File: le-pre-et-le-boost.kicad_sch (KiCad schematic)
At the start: 17 parts, among them J1 Power In, J2 IN, J3 OUT, Q1 MMBFJ201, Q2 MMBT5088

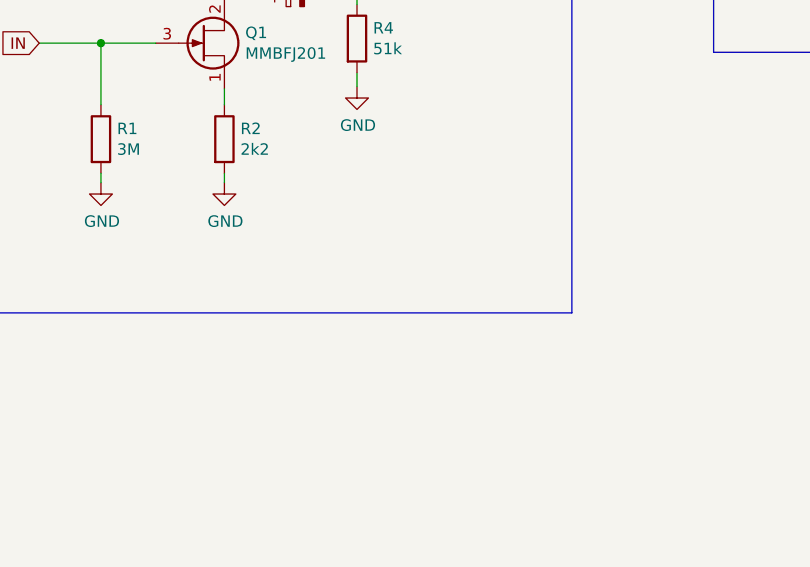
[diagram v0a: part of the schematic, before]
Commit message: some position and silkscreen adjustments
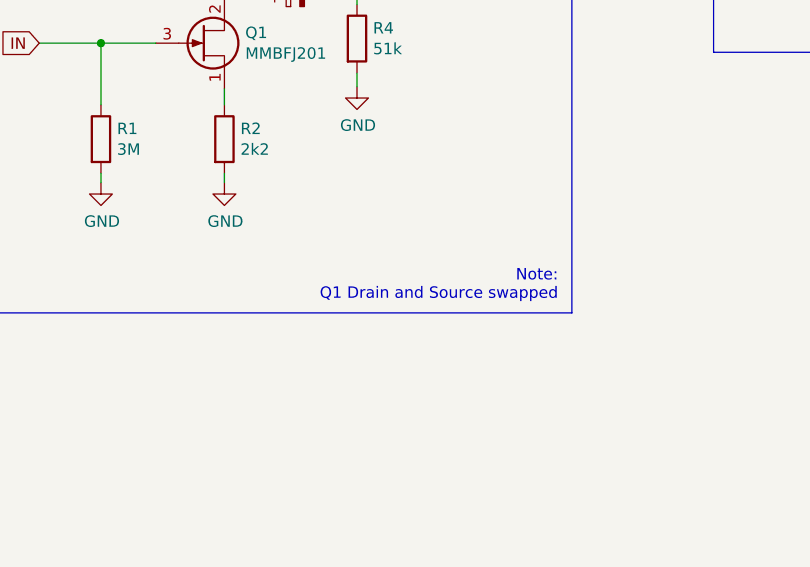
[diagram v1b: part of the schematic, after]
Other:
- note added: "Note: Q1 Drain and Source swapped"
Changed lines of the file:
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@@
+    (effects (font (size 1.27 1.27)) (justify right bottom))
+  )
+  (text "Note:\nQ1 Drain and Source swapped" (at 153.924 130.302 180)
     (effects (font (size 1.27 1.27)) (justify right bottom))
   )

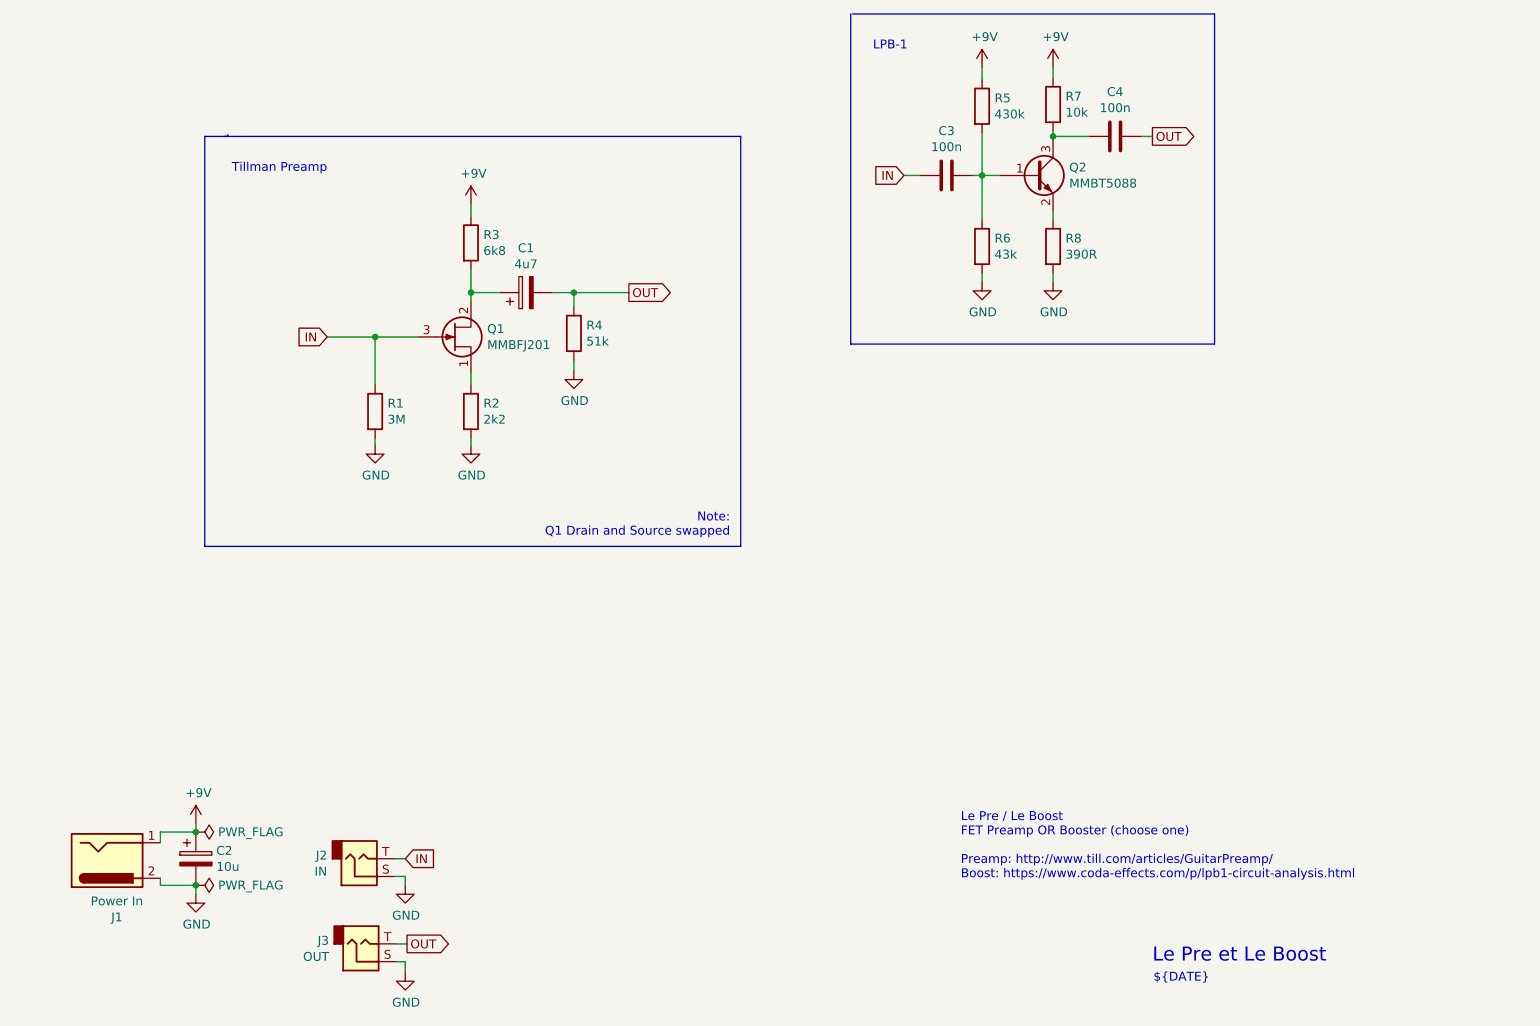
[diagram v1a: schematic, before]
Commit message: v0.2: THT footprints for electrolytics
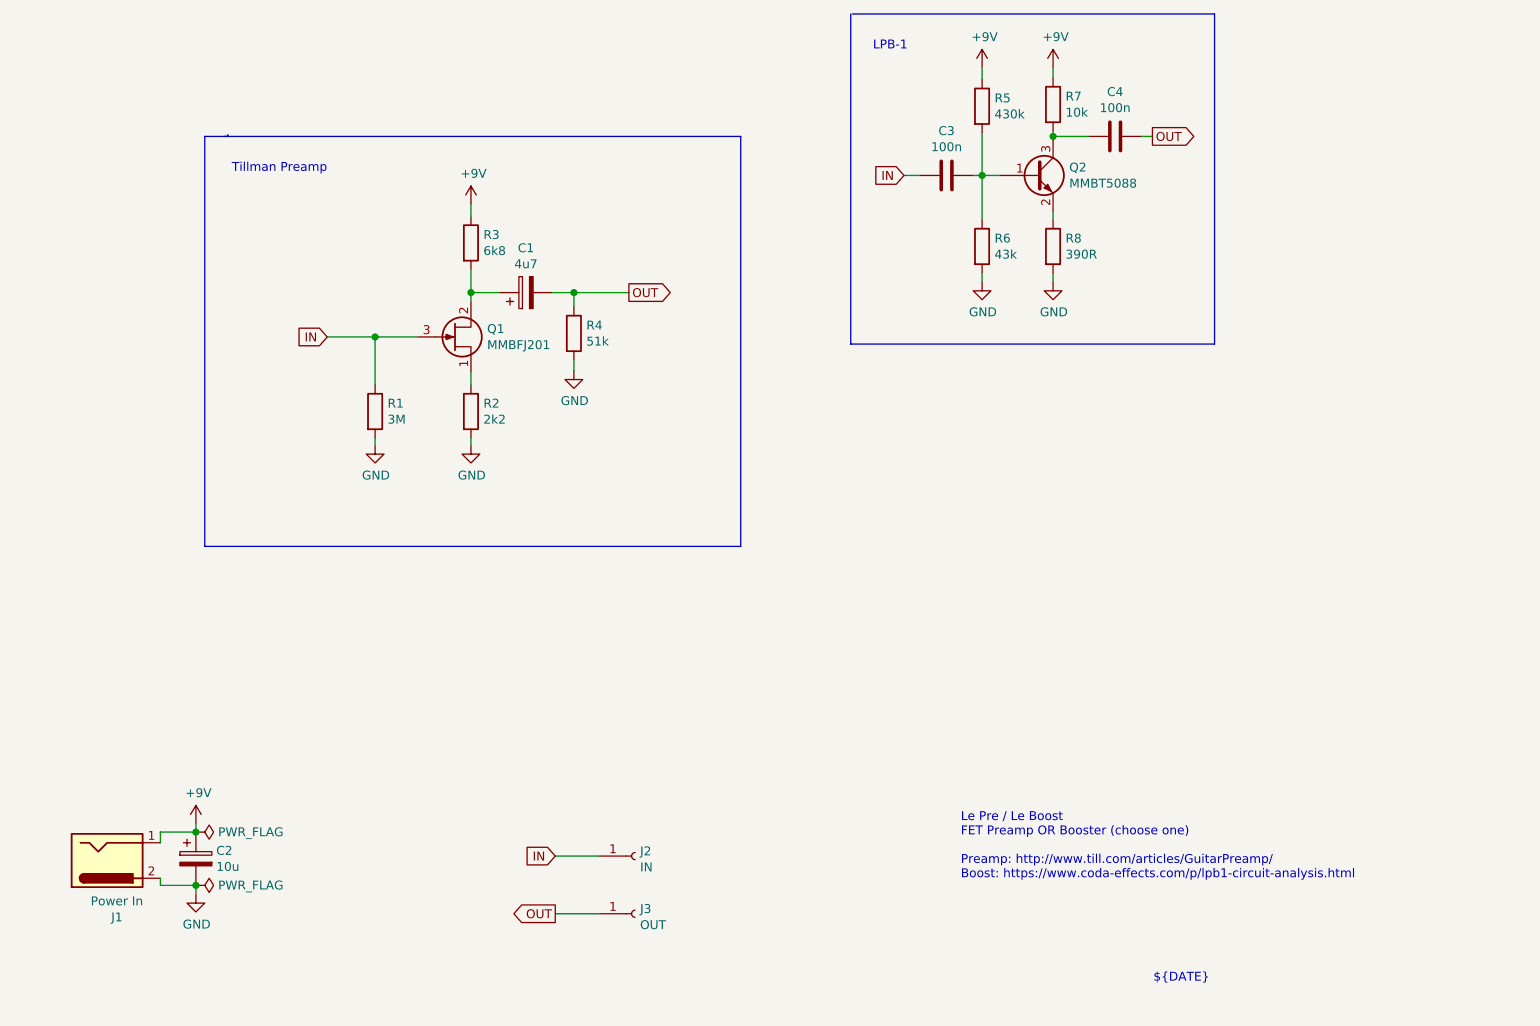
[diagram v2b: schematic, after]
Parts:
- removed J2: IN, rockola_kicad_footprints:2PADS_TS_Horizontal, symbol Connector:AudioJack2
- removed J3: OUT, rockola_kicad_footprints:2PADS_TS_Horizontal, symbol Connector:AudioJack2
- added J2: IN, rockola_kicad_footprints:Pin_1x01_P2.54mm, symbol Connector:Conn_01x01_Female
- added J3: OUT, rockola_kicad_footprints:Pin_1x01_P2.54mm, symbol Connector:Conn_01x01_Female
- C1, C2: footprint Capacitor_SMD:C_0805_2012Metric -> Capacitor_THT:CP_Radial_D5.0mm_P2.50mm
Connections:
- net IN: now also J2.1 (Pin_1)
- net OUT: now also J3.1 (Pin_1)
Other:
- note added: "${TITLE}"
- note removed: "Le Pre et Le Boost"
- note removed: "Note: Q1 Drain and Source swapped"
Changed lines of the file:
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@@
-(kicad_sch (version 20200714) (host eeschema "(5.99.0-2363-g9a801d8b7)")
+(kicad_sch (version 20200827) (generator eeschema)
   (page 1 1)
   (paper "A4")
-  (junction (at 77.47 172.466) (diameter 0) (color 0 0 0 0))
-  (junction (at 77.47 180.086) (diameter 0) (color 0 0 0 0))
-  (junction (at 103.124 101.6) (diameter 0) (color 0 0 0 0))
-  (junction (at 116.84 95.25) (diameter 0) (color 0 0 0 0))
-  (junction (at 131.572 95.25) (diameter 0) (color 0 0 0 0))
-  (junction (at 189.992 78.486) (diameter 0) (color 0 0 0 0))
-  (junction (at 200.152 72.898) (diameter 0) (color 0 0 0 0))
+  (junction (at 77.47 172.466) (diameter 1.016) (color 0 0 0 0))
+  (junction (at 77.47 180.086) (diameter 1.016) (color 0 0 0 0))
+  (junction (at 103.124 101.6) (diameter 1.016) (color 0 0 0 0))
+  (junction (at 116.84 95.25) (diameter 1.016) (color 0 0 0 0))
+  (junction (at 131.572 95.25) (diameter 1.016) (color 0 0 0 0))
+  (junction (at 189.992 78.486) (diameter 1.016) (color 0 0 0 0))
+  (junction (at 200.152 72.898) (diameter 1.016) (color 0 0 0 0))
   (wire (pts (xy 72.39 172.466) (xy 72.39 173.99))
     (stroke (width 0) (type solid) (color 0 0 0 0))
@@
     (stroke (width 0) (type solid) (color 0 0 0 0))
   )
-  (wire (pts (xy 105.918 176.276) (xy 107.442 176.276))
-    (stroke (width 0) (type solid) (color 0 0 0 0))
-  )
-  (wire (pts (xy 105.918 178.816) (xy 107.442 178.816))
-    (stroke (width 0) (type solid) (color 0 0 0 0))
-  )
-  (wire (pts (xy 106.172 188.468) (xy 107.696 188.468))
-    (stroke (width 0) (type solid) (color 0 0 0 0))
-  )
-  (wire (pts (xy 107.442 180.086) (xy 107.442 178.816))
-    (stroke (width 0) (type solid) (color 0 0 0 0))
-  )
-  (wire (pts (xy 107.442 191.008) (xy 106.172 191.008))
-    (stroke (width 0) (type solid) (color 0 0 0 0))
-  )
-  (wire (pts (xy 107.442 192.532) (xy 107.442 191.008))
-    (stroke (width 0) (type solid) (color 0 0 0 0))
-  )
   (wire (pts (xy 116.84 82.55) (xy 116.84 84.328))
     (stroke (width 0) (type solid) (color 0 0 0 0))
@@
     (stroke (width 0) (type solid) (color 0 0 0 0))
   )
+  (wire (pts (xy 128.905 175.895) (xy 135.255 175.895))
+    (stroke (width 0) (type solid) (color 0 0 0 0))
+  )
+  (wire (pts (xy 128.905 184.15) (xy 135.255 184.15))
+    (stroke (width 0) (type solid) (color 0 0 0 0))
+  )
   (wire (pts (xy 131.572 95.25) (xy 128.524 95.25))
     (stroke (width 0) (type solid) (color 0 0 0 0))
@@
   )
   (text "Tillman Preamp\n" (at 96.266 78.232 180)
-    (effects (font (size 1.27 1.27)) (justify right bottom))
-  )
-  (text "Note:\nQ1 Drain and Source swapped" (at 153.924 130.302 180)
     (effects (font (size 1.27 1.27)) (justify right bottom))
   )
@@
     (effects (font (size 1.27 1.27)) (justify right bottom))
   )
-  (text "Le Pre et Le Boost" (at 239.268 191.3382 180)
+  (text "${TITLE}" (at 239.268 191.3382 180)
     (effects (font (size 2 2)) (justify right bottom))
   )
@@
     (effects (font (size 1.27 1.27)) (justify right))
   )
-  (global_label "IN" (shape input) (at 107.442 176.276 0)
-    (effects (font (size 1.27 1.27)) (justify left))
-  )
-  (global_label "OUT" (shape output) (at 107.696 188.468 0)
-    (effects (font (size 1.27 1.27)) (justify left))
+  (global_label "IN" (shape input) (at 128.905 175.895 180)
+    (effects (font (size 1.27 1.27)) (justify right))
+  )
+  (global_label "OUT" (shape output) (at 128.905 184.15 180)
+    (effects (font (size 1.27 1.27)) (justify right))
   )
   (global_label "OUT" (shape output) (at 139.446 95.25 0)
@@
     )
   )
-  (symbol (lib_id "power:GND") (at 107.442 180.086 0) (unit 1)
-    (in_bom yes) (on_board yes)
-    (property "Reference" "#PWR05" (id 0) (at 107.442 186.436 0)
-      (effects (font (size 1.27 1.27)) hide)
-    )
-    (property "Value" "GND" (id 1) (at 107.5563 184.4104 0))
-    (property "Footprint" "" (id 2) (at 107.442 180.086 0)
-      (effects (font (size 1.27 1.27)) hide)
-    )
-    (property "Datasheet" "" (id 3) (at 107.442 180.086 0)
-      (effects (font (size 1.27 1.27)) hide)
-    )
-  )
-  (symbol (lib_id "power:GND") (at 107.442 192.532 0) (unit 1)
-    (in_bom yes) (on_board yes)
-    (property "Reference" "#PWR06" (id 0) (at 107.442 198.882 0)
-      (effects (font (size 1.27 1.27)) hide)
-    )
-    (property "Value" "GND" (id 1) (at 107.5563 196.8564 0))
-    (property "Footprint" "" (id 2) (at 107.442 192.532 0)
-      (effects (font (size 1.27 1.27)) hide)
-    )
-    (property "Datasheet" "" (id 3) (at 107.442 192.532 0)
-      (effects (font (size 1.27 1.27)) hide)
-    )
-  )
   (symbol (lib_id "power:GND") (at 116.84 117.094 0) (unit 1)
     (in_bom yes) (on_board yes)
@@
     )
   )
+  (symbol (lib_id "Connector:Conn_01x01_Female") (at 140.335 175.895 0) (unit 1)
+    (in_bom yes) (on_board yes)
+    (property "Reference" "J2" (id 0) (at 141.046 175.203 0)
+      (effects (font (size 1.27 1.27)) (justify left))
+    )
+    (property "Value" "IN" (id 1) (at 141.046 177.502 0)
+      (effects (font (size 1.27 1.27)) (justify left))
+    )
+    (property "Footprint" "rockola_kicad_footprints:Pin_1x01_P2.54mm" (id 2) (at 140.335 175.895 0)
+      (effects (font (size 1.27 1.27)) hide)
+    )
+    (property "Datasheet" "~" (id 3) (at 140.335 175.895 0)
+      (effects (font (size 1.27 1.27)) hide)
+    )
+  )
+  (symbol (lib_id "Connector:Conn_01x01_Female") (at 140.335 184.15 0) (unit 1)
+    (in_bom yes) (on_board yes)
+    (property "Reference" "J3" (id 0) (at 141.046 183.458 0)
+      (effects (font (size 1.27 1.27)) (justify left))
+    )
+    (property "Value" "OUT" (id 1) (at 141.046 185.757 0)
+      (effects (font (size 1.27 1.27)) (justify left))
+    )
+    (property "Footprint" "rockola_kicad_footprints:Pin_1x01_P2.54mm" (id 2) (at 140.335 184.15 0)
+      (effects (font (size 1.27 1.27)) hide)
+    )
+    (property "Datasheet" "~" (id 3) (at 140.335 184.15 0)
+      (effects (font (size 1.27 1.27)) hide)
+    )
+  )
   (symbol (lib_id "Device:R") (at 103.124 112.268 0) (unit 1)
     (in_bom yes) (on_board yes)
@@
       (effects (font (size 1.27 1.27)) (justify left))
     )
-    (property "Footprint" "Capacitor_SMD:C_0805_2012Metric" (id 2) (at 78.4352 180.086 0)
+    (property "Footprint" "Capacitor_THT:CP_Radial_D5.0mm_P2.50mm" (id 2) (at 78.4352 180.086 0)
       (effects (font (size 1.27 1.27)) hide)
     )
@@
     (property "Reference" "C1" (id 0) (at 124.714 88.8808 90))
     (property "Value" "4u7" (id 1) (at 124.714 91.1795 90))
-    (property "Footprint" "Capacitor_SMD:C_0805_2012Metric" (id 2) (at 128.524 94.2848 0)
+    (property "Footprint" "Capacitor_THT:CP_Radial_D5.0mm_P2.50mm" (id 2) (at 128.524 94.2848 0)
       (effects (font (size 1.27 1.27)) hide)
     )
@@
     )
   )
-  (symbol (lib_id "Connector:AudioJack2") (at 100.838 176.276 0) (mirror x) (unit 1)
-    (in_bom yes) (on_board yes)
-    (property "Reference" "J2" (id 0) (at 96.2659 175.8124 0)
-      (effects (font (size 1.27 1.27)) (justify right))
-    )
-    (property "Value" "IN" (id 1) (at 96.2659 178.1111 0)
-      (effects (font (size 1.27 1.27)) (justify right))
-    )
-    (property "Footprint" "rockola_kicad_footprints:2PADS_TS_Horizontal" (id 2) (at 100.838 176.276 0)
-      (effects (font (size 1.27 1.27)) hide)
-    )
-    (property "Datasheet" "~" (id 3) (at 100.838 176.276 0)
-      (effects (font (size 1.27 1.27)) hide)
-    )
-  )
-  (symbol (lib_id "Connector:AudioJack2") (at 101.092 188.468 0) (mirror x) (unit 1)
-    (in_bom yes) (on_board yes)
-    (property "Reference" "J3" (id 0) (at 96.5199 188.0044 0)
-      (effects (font (size 1.27 1.27)) (justify right))
-    )
-    (property "Value" "OUT" (id 1) (at 96.5199 190.3031 0)
-      (effects (font (size 1.27 1.27)) (justify right))
-    )
-    (property "Footprint" "rockola_kicad_footprints:2PADS_TS_Horizontal" (id 2) (at 101.092 188.468 0)
-      (effects (font (size 1.27 1.27)) hide)
-    )
-    (property "Datasheet" "~" (id 3) (at 101.092 188.468 0)
-      (effects (font (size 1.27 1.27)) hide)
-    )
-  )
   (symbol (lib_id "rockola_symbols:Power_Pedal_BarrelJack") (at 64.77 176.53 0) (mirror x) (unit 1)
     (in_bom yes) (on_board yes)
@@
       (reference "#PWR04") (unit 1)
     )
-    (path "/a854a22f-258e-4ae3-a023-31ac1b1c42e5"
-      (reference "#PWR05") (unit 1)
-    )
-    (path "/951c042a-e8ad-4a92-998e-2421dc76a319"
-      (reference "#PWR06") (unit 1)
-    )
     (path "/17b1b474-45b5-49ba-95bd-5c83f5e1aa64"
       (reference "#PWR07") (unit 1)
@@
       (reference "J1") (unit 1)
     )
-    (path "/2e8722fc-d95d-4be7-b823-0909b168c330"
+    (path "/80577a87-c6aa-4063-867e-5814fcb65860"
       (reference "J2") (unit 1)
     )
-    (path "/dd44408d-8ccd-4ec4-9826-2477b3952ac8"
+    (path "/9be21875-065d-4d50-9c34-532f5b30e076"
       (reference "J3") (unit 1)
     )

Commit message: v0.3: separate in/out for both sides
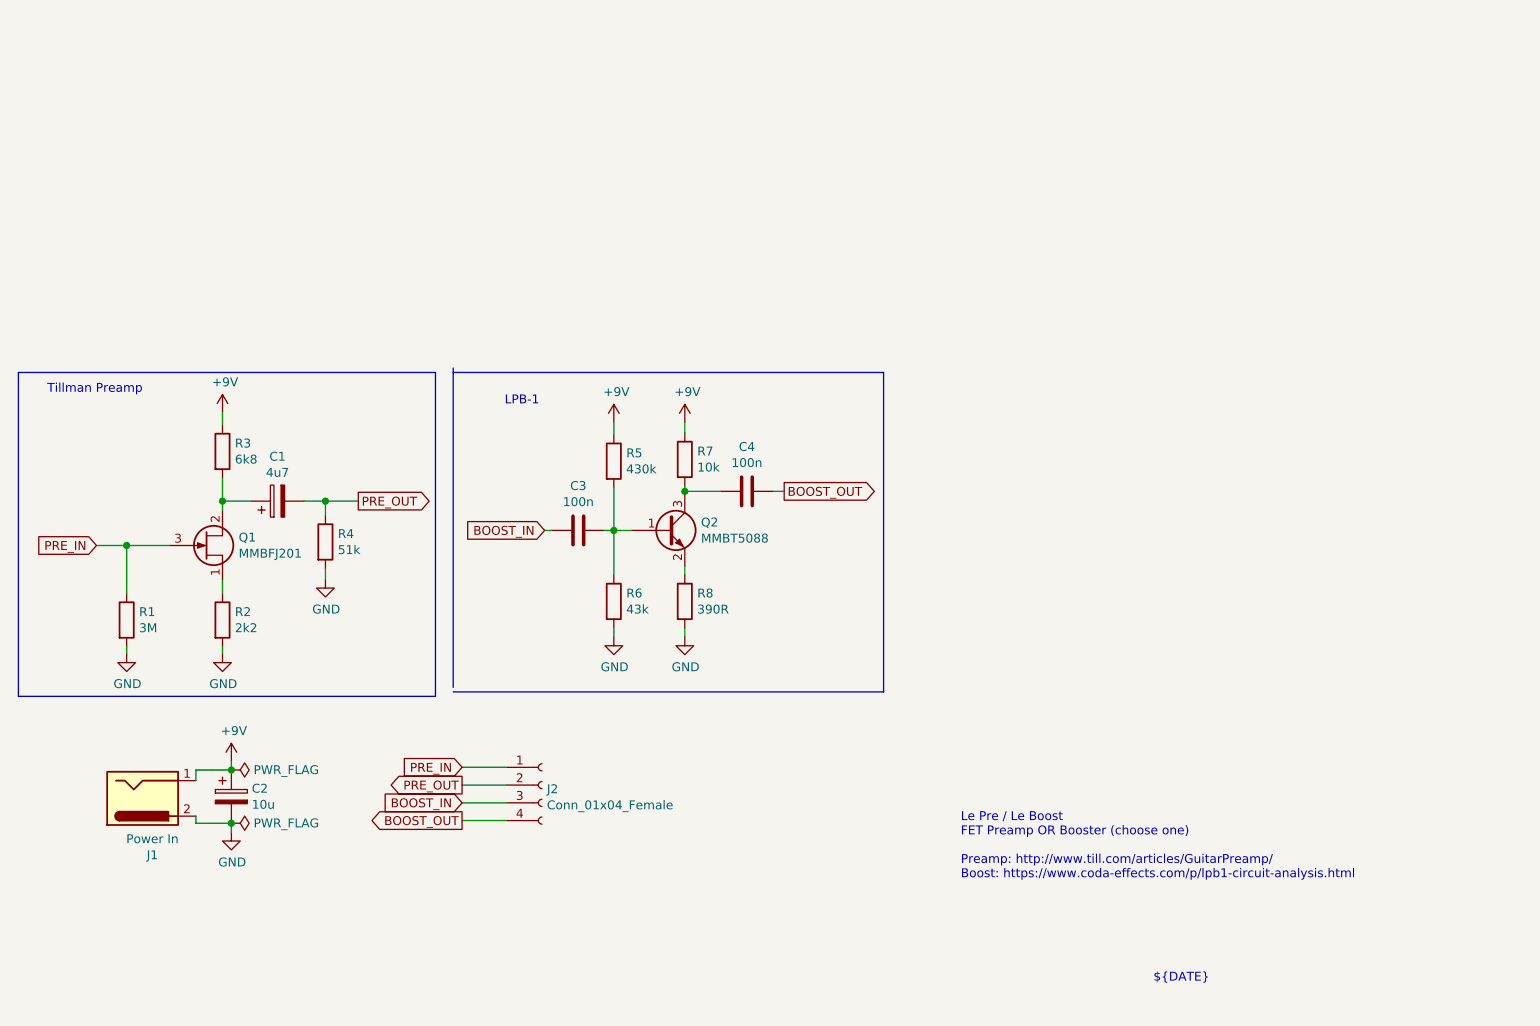
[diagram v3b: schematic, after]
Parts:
- removed J2: IN, rockola_kicad_footprints:Pin_1x01_P2.54mm, symbol Connector:Conn_01x01_Female
- removed J3: OUT, rockola_kicad_footprints:Pin_1x01_P2.54mm, symbol Connector:Conn_01x01_Female
- added J2: Conn_01x04_Female, rockola_kicad_footprints:Stomp_4pin_ALT2, symbol Connector:Conn_01x04_Female
- C1, C2: footprint Capacitor_THT:CP_Radial_D5.0mm_P2.50mm -> rockola_kicad_footprints:CP_D5.0_P2.50
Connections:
- net IN renamed PRE_IN
- net PRE_IN: now also J2.1 (Pin_1); no longer C3.1
- net OUT renamed PRE_OUT
- net PRE_OUT: now also J2.2 (Pin_2); no longer C4.2
- new net BOOST_IN: C3.1, J2.3 (Pin_3)
- new net BOOST_OUT: C4.2, J2.4 (Pin_4)
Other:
- moved on the sheet: C1, C2, C3, C4, J1, Q1, Q2, R1, R2, R3, R4, R5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
